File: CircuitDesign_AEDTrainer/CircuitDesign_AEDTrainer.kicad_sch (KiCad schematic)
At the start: 11 parts, among them SW1 SW_Rotary_1x6_MP, SW2 SW_Push, SW3 SW_Push, U1 RP2040, U2 MAX98357AETE_T, U3 MICROSD_SPI_OR_SDIO_CARD

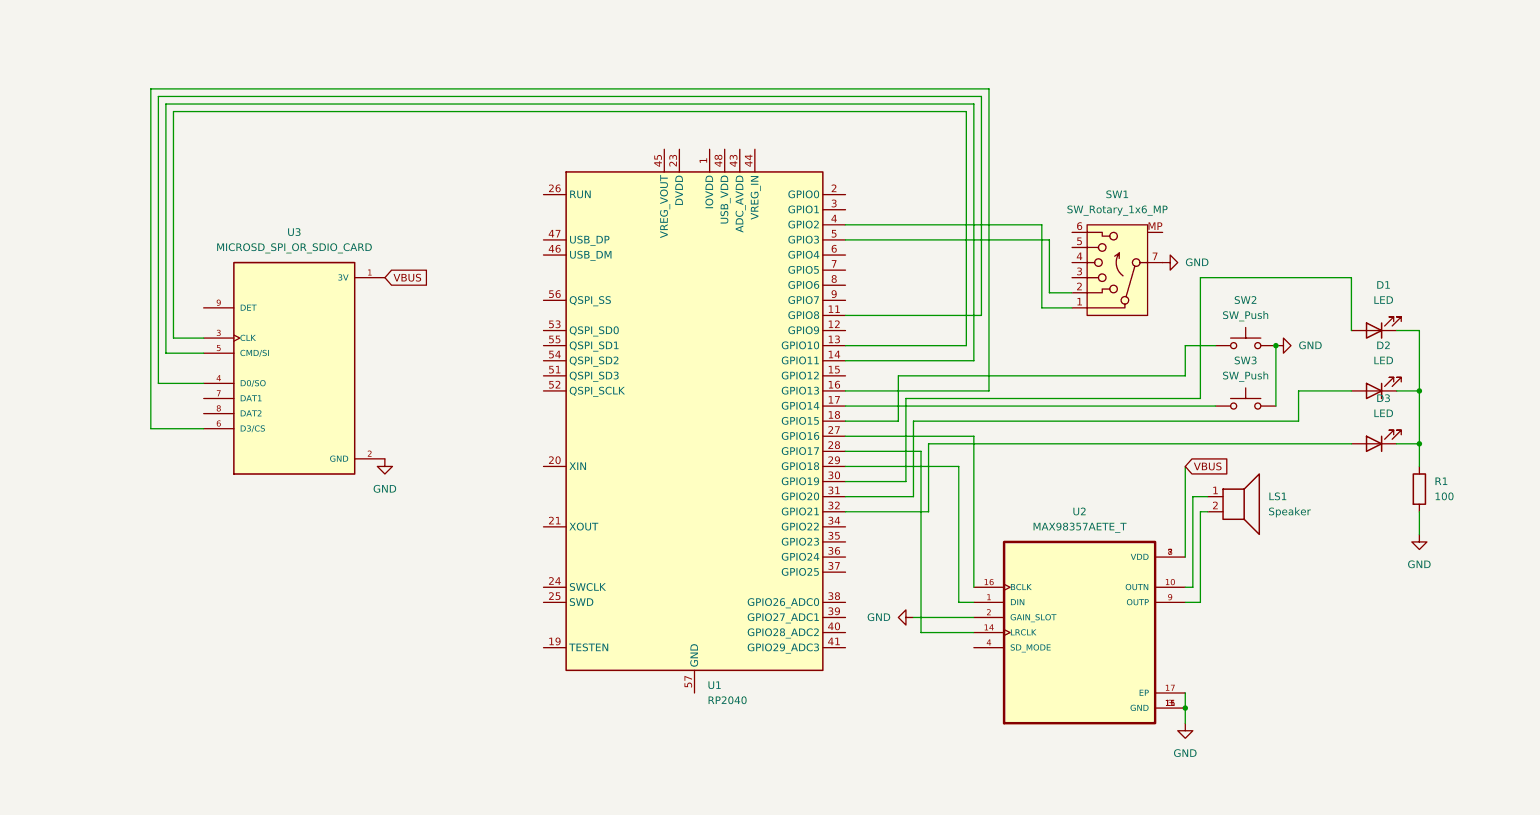
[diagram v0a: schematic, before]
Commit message: Schematics done, Footprints assigned
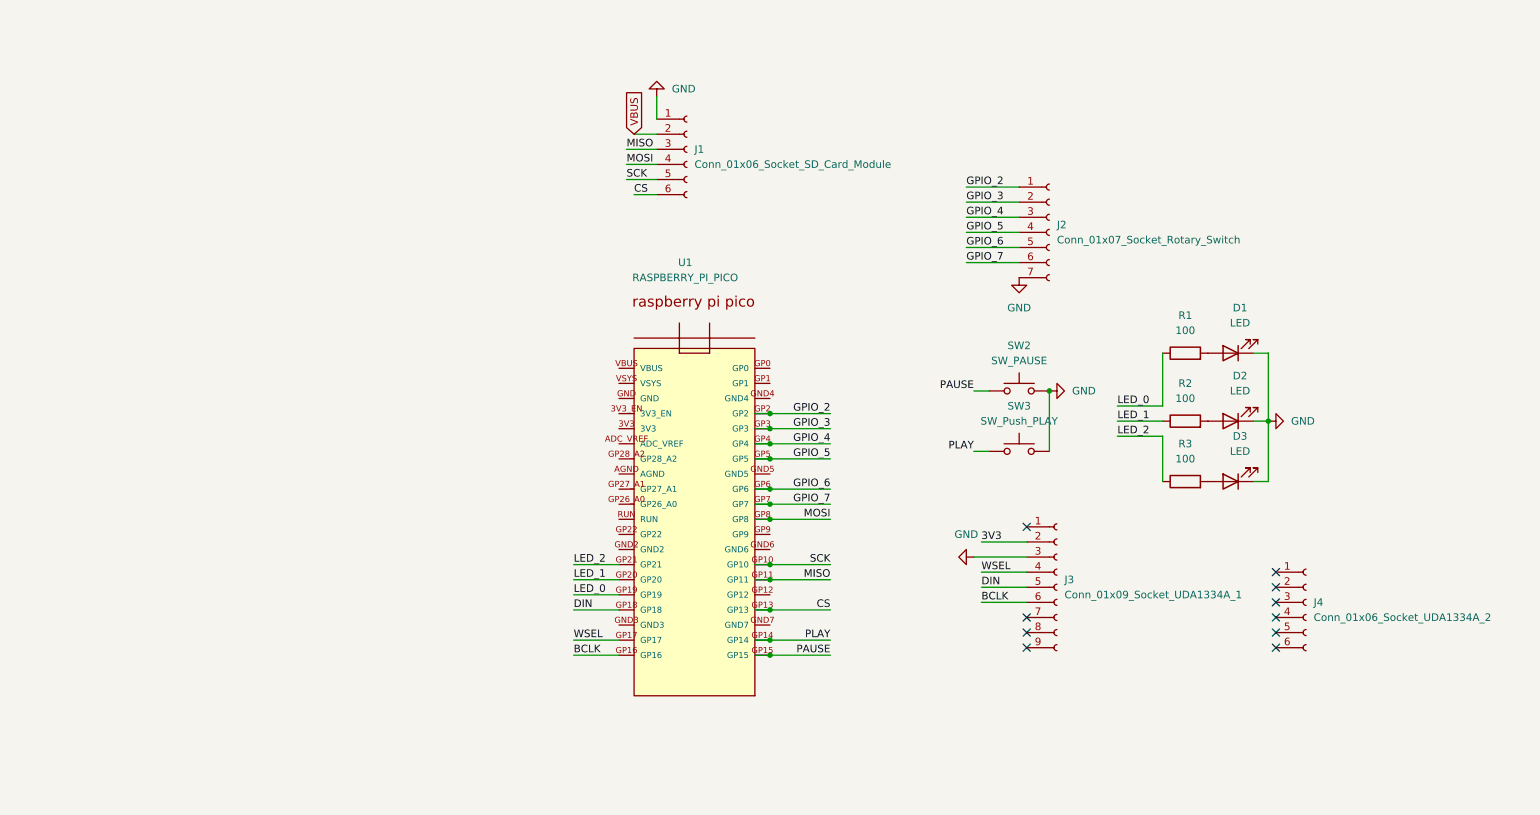
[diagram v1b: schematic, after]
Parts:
- removed LS1: Speaker, symbol Device:Speaker
- removed SW1: SW_Rotary_1x6_MP, symbol Switch:SW_Rotary_1x6_MP
- removed U1: RP2040, Package_DFN_QFN:QFN-56-1EP_7x7mm_P0.4mm_EP3.2x3.2mm, symbol MCU_RaspberryPi:RP2040
- removed U2: MAX98357AETE_T, MAX98357AETE_T:QFN50P300X300X80-17N, symbol MAX98357AETE_T:MAX98357AETE_T
- removed U3: MICROSD_SPI_OR_SDIO_CARD, MICROSD_SPI_OR_SDIO_CARD:MODULE_MICROSD_SPI_OR_SDIO_CARD, symbol MICROSD_SPI_OR_SDIO_CARD:MICROSD_SPI_OR_SDIO_CARD
- added J1: Conn_01x06_Socket_SD_Card_Module, Connector_PinSocket_2.54mm:PinSocket_1x06_P2.54mm_Horizontal, symbol Connector:Conn_01x06_Socket
- added J2: Conn_01x07_Socket_Rotary_Switch, Connector_JST:JST_XH_B7B-XH-A_1x07_P2.50mm_Vertical, symbol Connector:Conn_01x07_Socket
- added J3: Conn_01x09_Socket_UDA1334A_1, Connector_PinSocket_2.54mm:PinSocket_1x09_P2.54mm_Vertical, symbol Connector:Conn_01x09_Socket
- added J4: Conn_01x06_Socket_UDA1334A_2, Connector_PinSocket_2.54mm:PinSocket_1x06_P2.54mm_Vertical, symbol Connector:Conn_01x06_Socket
- added R2, R3: 100, Resistor_THT:R_Axial_DIN0309_L9.0mm_D3.2mm_P15.24mm_Horizontal, symbol Device:R
- added U1: RASPBERRY_PI_PICO, RPI_Pico:RASPBERRY_PI_PICO, symbol RASPBERRY_PI_PICO:RASPBERRY_PI_PICO
- D1, D2, D3: footprint (none) -> LED_THT:LED_D3.0mm
- R1: footprint (none) -> Resistor_THT:R_Axial_DIN0309_L9.0mm_D3.2mm_P15.24mm_Horizontal
- SW2: value SW_Push -> SW_PAUSE; footprint (none) -> Button_Switch_THT:SW_Tactile_Straight_KSL0Axx1LFTR
- SW3: value SW_Push -> SW_Push_PLAY; footprint (none) -> Button_Switch_THT:SW_Tactile_Straight_KSL0Axx1LFTR
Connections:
- net GND: now also D1.1 (K), D2.1 (K), D3.1 (K), J1.1 (Pin_1), J2.7 (Pin_7), J3.3 (Pin_3); no longer R1.2
- net VBUS: now also J1.2 (Pin_2)
- net PAUSE: now reaches SW2.1
- net PAUSE: now also U1.GP15
- net PLAY: now reaches SW3.1
- net PLAY: now also U1.GP14
- net at D3.2 (A): now also R3.2
- net at D2.2 (A): now also R2.2
- net at D1.2 (A): now also R1.2
- new net 3V3: J3.2 (Pin_2)
- new net BCLK: J3.6 (Pin_6), U1.GP16
- new net CS: J1.6 (Pin_6), U1.GP13
- new net DIN: J3.5 (Pin_5), U1.GP18
- new net GPIO_2: J2.1 (Pin_1), U1.GP2
- new net GPIO_3: J2.2 (Pin_2), U1.GP3
- new net GPIO_4: J2.3 (Pin_3), U1.GP4
- new net GPIO_5: J2.4 (Pin_4), U1.GP5
- new net GPIO_6: J2.5 (Pin_5), U1.GP6
- new net GPIO_7: J2.6 (Pin_6), U1.GP7
- new net LED_0: R1.1, U1.GP19
- new net LED_1: R2.1, U1.GP20
- new net LED_2: R3.1, U1.GP21
- new net MISO: J1.3 (Pin_3), U1.GP11
- new net MOSI: J1.4 (Pin_4), U1.GP8
- new net SCK: J1.5 (Pin_5), U1.GP10
- new net WSEL: J3.4 (Pin_4), U1.GP17
- no-connect marks 0 -> 10
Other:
- moved on the sheet: SW2, SW3

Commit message: Layout done
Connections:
- net 3V3: now also U1.3V3
- net GND: now also U1.GND, U1.GND2, U1.GND3, U1.GND4, U1.GND5, U1.GND6, U1.GND7
- net VBUS: now also U1.VBUS
- no-connect marks 10 -> 23
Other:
- note added: "Instruction Index Indicator LEDs"
- note added: "Language Selection Rotary Switch"
- note added: "Micro SD Card Module"
- note added: "Play & Pause Tactile Switches"
- note added: "Raspberry Pi Pico - Microcontroller Board"
- note added: "UDA1334A I2S DAC Board"
- title: (none) -> AED Trainer Kit - Circuit Design
- moved on the sheet: D1, D2, D3, J1, J2, J3, J4, R1, R2, R3, SW2, SW3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

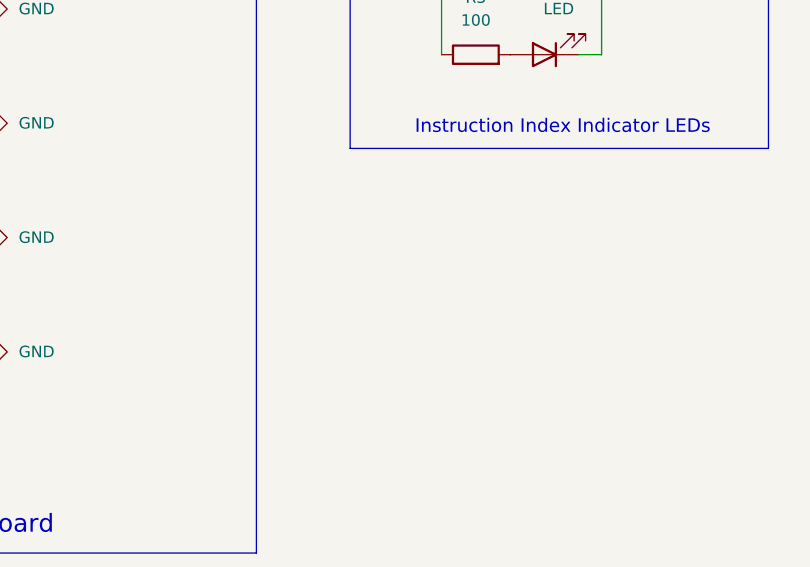
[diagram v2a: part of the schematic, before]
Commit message: Schematic change for SD Card
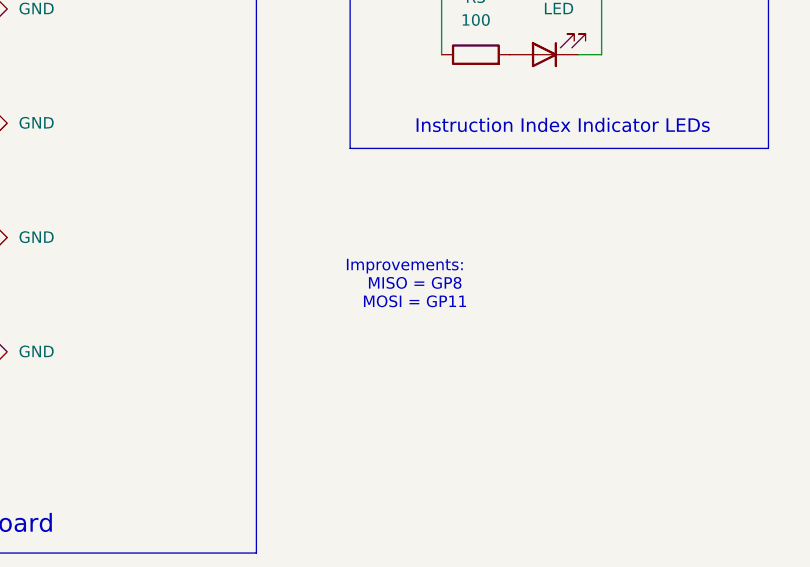
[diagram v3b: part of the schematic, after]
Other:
- note added: "Improvements: MISO = GP8 MOSI = GP11"
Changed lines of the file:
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@@
+		)
+	)
+	(text "Improvements:\n	MISO = GP8\n	MOSI = GP11\n"
+		(exclude_from_sim no)
+		(at 157.226 123.444 0)
+		(effects
+			(font
+				(size 1.27 1.27)
+			)
 		)
 	)
